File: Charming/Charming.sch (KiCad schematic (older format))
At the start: 9 parts, among them U1 proton_c

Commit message: sym4
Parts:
- removed U1: proton_c, symbol proton_c:proton_c
- added U1: ProMicro, Keebio-Parts:ArduinoProMicro, symbol keebio:ProMicro
- D1, D2, D3, D4: renamed from D?; footprint (none) -> Diode_SMD:D_SOD-123
- SW1, SW2, SW3, SW4: renamed from SW?; footprint (none) -> keyswitches:SW_PG1350
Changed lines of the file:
@@
 Comment4 ""
 $EndDescr
-$Comp
-L proton_c:proton_c U1
-U 1 1 5EE8D2D3
-P 2800 2100
-F 0 "U1" H 2775 577 50  0000 C CNN
-F 1 "proton_c" H 2775 486 50  0000 C CNN
-F 2 "" H 2650 2100 50  0001 C CNN
-F 3 "" H 2650 2100 50  0001 C CNN
-	1    2800 2100
-	1    0    0    -1
-$EndComp
 Wire Wire Line
 	4200 1400 3800 1400
@@
 L power:GND #PWR0102
 U 1 1 5EE91DD7
-P 1300 1600
-F 0 "#PWR0102" H 1300 1350 50  0001 C CNN
-F 1 "GND" H 1305 1427 50  0000 C CNN
-F 2 "" H 1300 1600 50  0001 C CNN
-F 3 "" H 1300 1600 50  0001 C CNN
-	1    1300 1600
-	1    0    0    -1
-$EndComp
-Wire Wire Line
-	1750 1300 1300 1300
-Wire Wire Line
-	1750 1400 1300 1400
-Wire Wire Line
-	1300 1300 1300 1400
+P 1950 1600
+F 0 "#PWR0102" H 1950 1350 50  0001 C CNN
+F 1 "GND" H 1955 1427 50  0000 C CNN
+F 2 "" H 1950 1600 50  0001 C CNN
+F 3 "" H 1950 1600 50  0001 C CNN
+	1    1950 1600
+	1    0    0    -1
+$EndComp
+Wire Wire Line
+	2400 1300 1950 1300
+Wire Wire Line
+	2400 1400 1950 1400
+Wire Wire Line
+	1950 1300 1950 1400
 $Comp
 L power:GND #PWR0103
@@
 L power:PWR_FLAG #FLG0102
 U 1 1 5EE952BC
-P 900 1650
-F 0 "#FLG0102" H 900 1725 50  0001 C CNN
-F 1 "PWR_FLAG" H 900 1823 50  0000 C CNN
-F 2 "" H 900 1650 50  0001 C CNN
-F 3 "~" H 900 1650 50  0001 C CNN
-	1    900  1650
+P 1550 1650
+F 0 "#FLG0102" H 1550 1725 50  0001 C CNN
+F 1 "PWR_FLAG" H 1550 1823 50  0000 C CNN
+F 2 "" H 1550 1650 50  0001 C CNN
+F 3 "~" H 1550 1650 50  0001 C CNN
+	1    1550 1650
 	1    0    0    -1
 $EndComp
@@
 	4200 1150 4200 1400
 Wire Wire Line
-	1300 1400 1300 1600
-Connection ~ 1300 1400
+	1950 1400 1950 1600
+Connection ~ 1950 1400
 $Comp
 L power:GND #PWR0104
 U 1 1 5EE95E75
-P 900 1750
-F 0 "#PWR0104" H 900 1500 50  0001 C CNN
-F 1 "GND" H 905 1577 50  0000 C CNN
-F 2 "" H 900 1750 50  0001 C CNN
-F 3 "" H 900 1750 50  0001 C CNN
-	1    900  1750
-	1    0    0    -1
-$EndComp
-Wire Wire Line
-	900  1650 900  1750
+P 1550 1750
+F 0 "#PWR0104" H 1550 1500 50  0001 C CNN
+F 1 "GND" H 1555 1577 50  0000 C CNN
+F 2 "" H 1550 1750 50  0001 C CNN
+F 3 "" H 1550 1750 50  0001 C CNN
+	1    1550 1750
+	1    0    0    -1
+$EndComp
+Wire Wire Line
+	1550 1650 1550 1750
 Wire Wire Line
 	4750 1250 4700 1250
@@
 	4750 900  4750 1250
 $Comp
-L Switch:SW_Push SW?
+L Switch:SW_Push SW1
 U 1 1 5EEA09FE
 P 4150 4900
-F 0 "SW?" H 4150 5185 50  0000 C CNN
+F 0 "SW1" H 4150 5185 50  0000 C CNN
 F 1 "SW_Push" H 4150 5094 50  0000 C CNN
-F 2 "" H 4150 5100 50  0001 C CNN
+F 2 "keyswitches:SW_PG1350" H 4150 5100 50  0001 C CNN
 F 3 "~" H 4150 5100 50  0001 C CNN
 	1    4150 4900
@@
 $EndComp
 $Comp
-L Switch:SW_Push SW?
+L Switch:SW_Push SW2
 U 1 1 5EEA0DB6
 P 4150 5600
-F 0 "SW?" H 4150 5885 50  0000 C CNN
+F 0 "SW2" H 4150 5885 50  0000 C CNN
 F 1 "SW_Push" H 4150 5794 50  0000 C CNN
-F 2 "" H 4150 5800 50  0001 C CNN
+F 2 "keyswitches:SW_PG1350" H 4150 5800 50  0001 C CNN
 F 3 "~" H 4150 5800 50  0001 C CNN
 	1    4150 5600
@@
 $EndComp
 $Comp
-L Switch:SW_Push SW?
+L Switch:SW_Push SW3
 U 1 1 5EEA10F4
 P 4900 4900
-F 0 "SW?" H 4900 5185 50  0000 C CNN
+F 0 "SW3" H 4900 5185 50  0000 C CNN
 F 1 "SW_Push" H 4900 5094 50  0000 C CNN
-F 2 "" H 4900 5100 50  0001 C CNN
+F 2 "keyswitches:SW_PG1350" H 4900 5100 50  0001 C CNN
 F 3 "~" H 4900 5100 50  0001 C CNN
 	1    4900 4900
@@
 $EndComp
 $Comp
-L Switch:SW_Push SW?
+L Switch:SW_Push SW4
 U 1 1 5EEA1601
 P 4900 5600
-F 0 "SW?" H 4900 5885 50  0000 C CNN
+F 0 "SW4" H 4900 5885 50  0000 C CNN
 F 1 "SW_Push" H 4900 5794 50  0000 C CNN
-F 2 "" H 4900 5800 50  0001 C CNN
+F 2 "keyswitches:SW_PG1350" H 4900 5800 50  0001 C CNN
 F 3 "~" H 4900 5800 50  0001 C CNN
 	1    4900 5600
@@
 	3950 4900 3950 5600
 $Comp
-L Device:D D?
+L Device:D D1
 U 1 1 5EEA2409
 P 4350 5050
-F 0 "D?" V 4396 4970 50  0000 R CNN
+F 0 "D1" V 4396 4970 50  0000 R CNN
 F 1 "D" V 4305 4970 50  0000 R CNN
-F 2 "" H 4350 5050 50  0001 C CNN
+F 2 "Diode_SMD:D_SOD-123" H 4350 5050 50  0001 C CNN
 F 3 "~" H 4350 5050 50  0001 C CNN
 	1    4350 5050
@@
 $EndComp
 $Comp
-L Device:D D?
+L Device:D D3
 U 1 1 5EEA2C67
 P 5100 5050
-F 0 "D?" V 5146 4970 50  0000 R CNN
+F 0 "D3" V 5146 4970 50  0000 R CNN
 F 1 "D" V 5055 4970 50  0000 R CNN
-F 2 "" H 5100 5050 50  0001 C CNN
+F 2 "Diode_SMD:D_SOD-123" H 5100 5050 50  0001 C CNN
 F 3 "~" H 5100 5050 50  0001 C CNN
 	1    5100 5050
@@
 $EndComp
 $Comp
-L Device:D D?
+L Device:D D2
 U 1 1 5EEA30D5
 P 4350 5750
-F 0 "D?" V 4396 5670 50  0000 R CNN
+F 0 "D2" V 4396 5670 50  0000 R CNN
 F 1 "D" V 4305 5670 50  0000 R CNN
-F 2 "" H 4350 5750 50  0001 C CNN
+F 2 "Diode_SMD:D_SOD-123" H 4350 5750 50  0001 C CNN
 F 3 "~" H 4350 5750 50  0001 C CNN
 	1    4350 5750
@@
 $EndComp
 $Comp
-L Device:D D?
+L Device:D D4
 U 1 1 5EEA33F4
 P 5100 5750
-F 0 "D?" V 5146 5670 50  0000 R CNN
+F 0 "D4" V 5146 5670 50  0000 R CNN
 F 1 "D" V 5055 5670 50  0000 R CNN
-F 2 "" H 5100 5750 50  0001 C CNN
+F 2 "Diode_SMD:D_SOD-123" H 5100 5750 50  0001 C CNN
 F 3 "~" H 5100 5750 50  0001 C CNN
 	1    5100 5750
@@
 Wire Wire Line
 	3800 1200 4350 1200
+Text GLabel 3800 1800 2    50   Input ~ 0
+col1
 Text GLabel 3800 1600 2    50   Input ~ 0
-col1
+row1
 Text GLabel 3800 1700 2    50   Input ~ 0
-row1
-Text GLabel 3800 1800 2    50   Input ~ 0
 col0
+$Comp
+L keebio:ProMicro U1
+U 1 1 5EEA488D
+P 3100 1650
+F 0 "U1" H 3100 2487 60  0000 C CNN
+F 1 "ProMicro" H 3100 2381 60  0000 C CNN
+F 2 "Keebio-Parts:ArduinoProMicro" V 4150 -850 60  0001 C CNN
+F 3 "" V 4150 -850 60  0001 C CNN
+	1    3100 1650
+	1    0    0    -1
+$EndComp
 $EndSCHEMATC

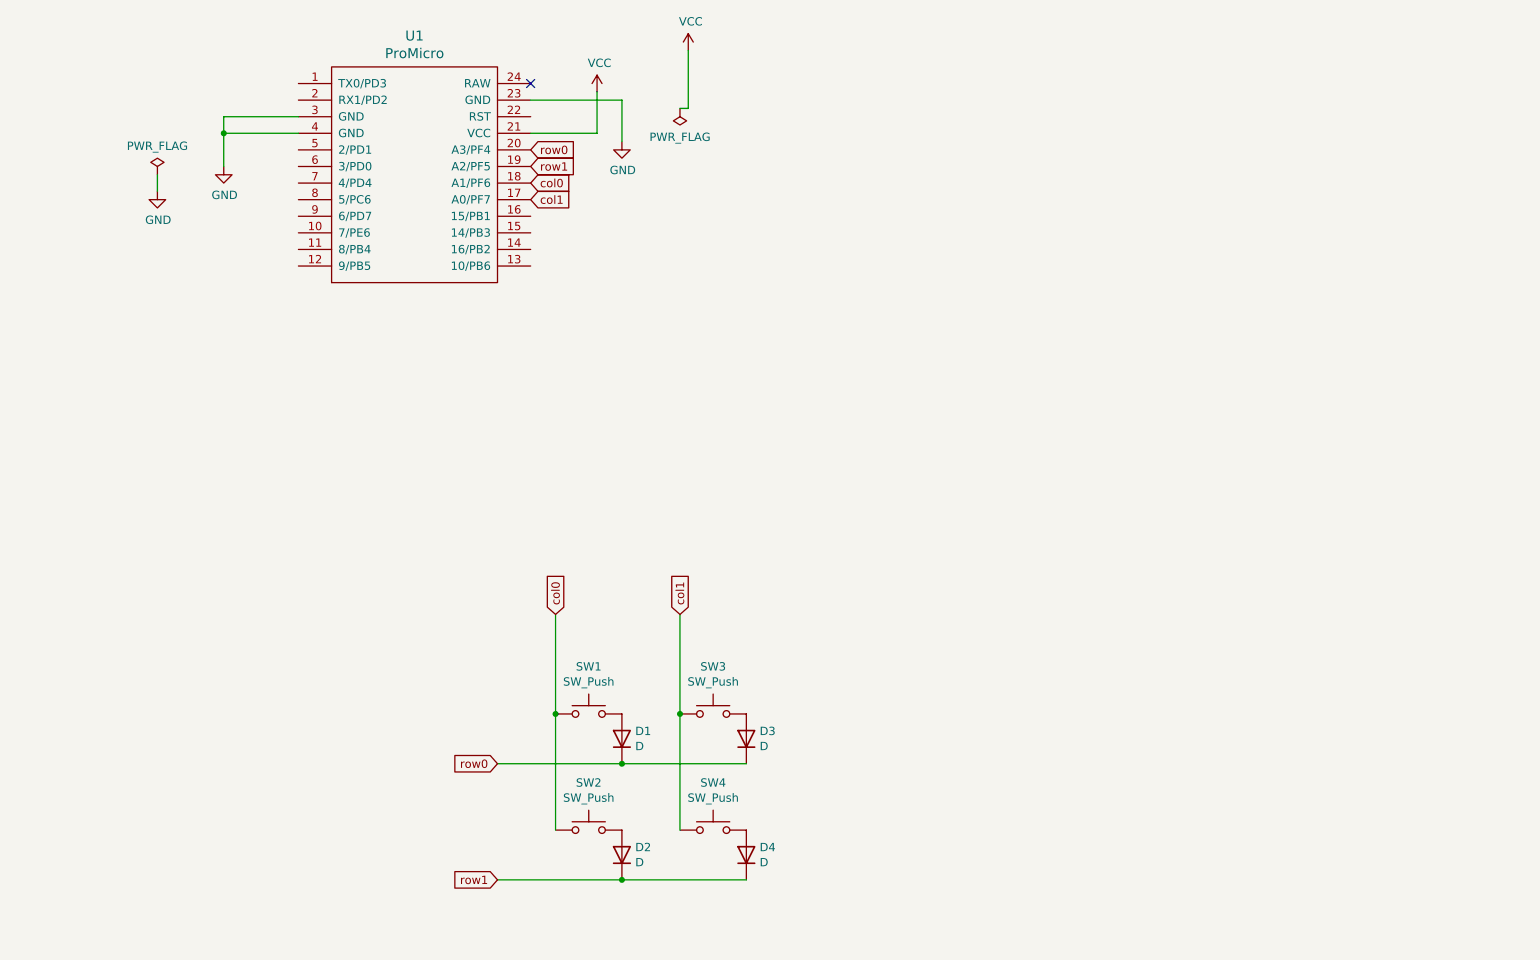
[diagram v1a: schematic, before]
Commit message: keyboard matrix ok
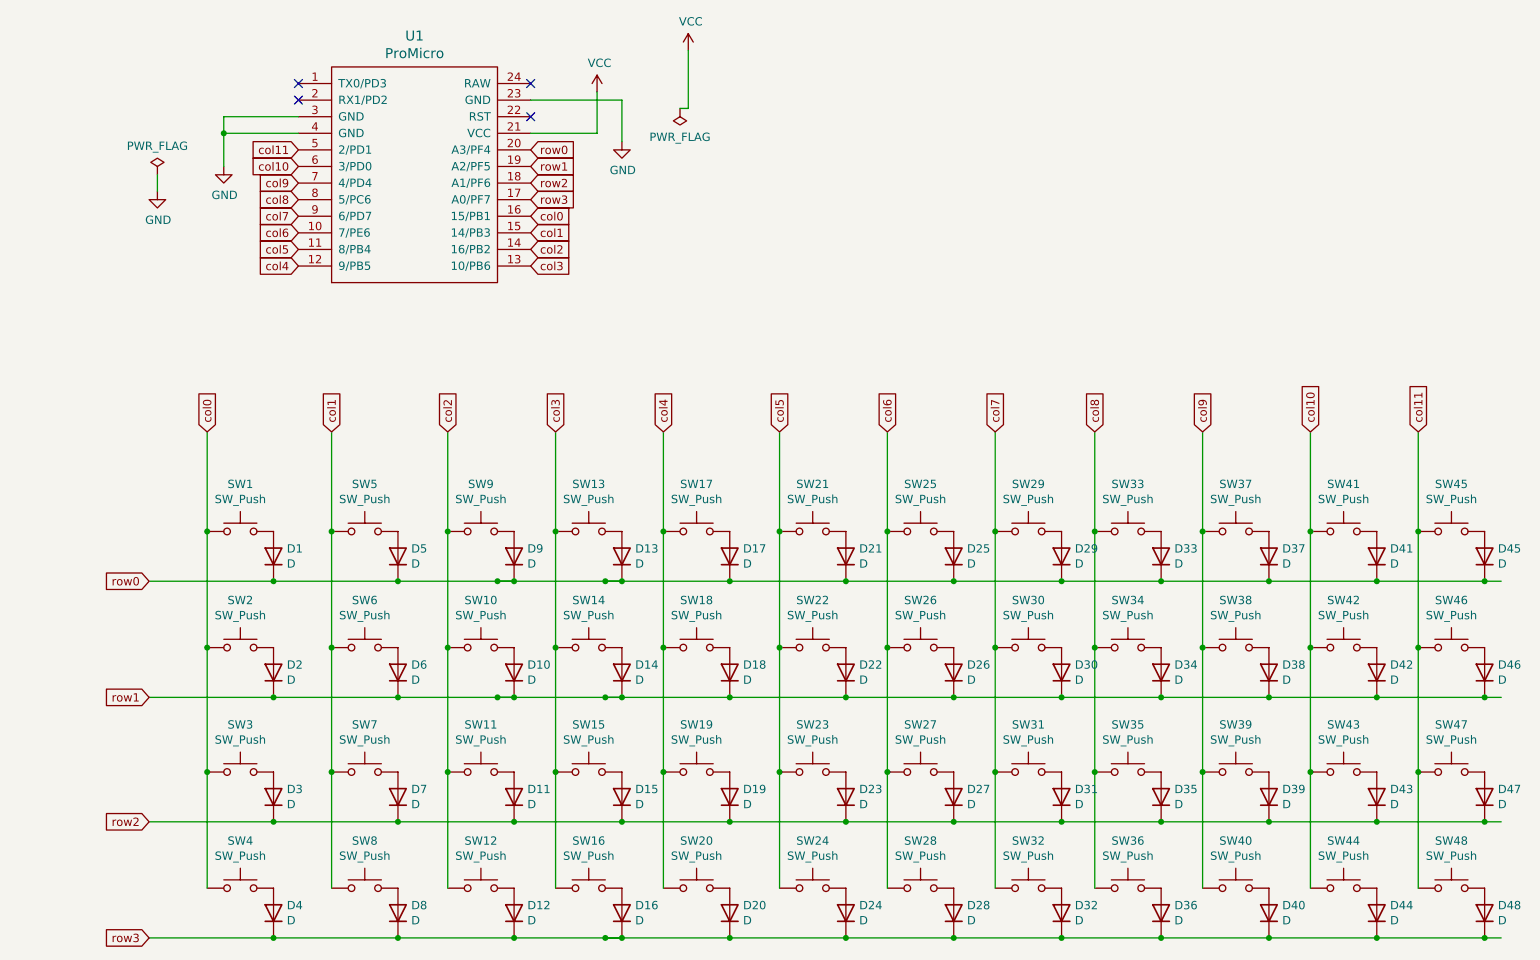
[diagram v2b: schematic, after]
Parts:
- added D10, D11, D12, D13, D14, D15, D16, D17, D18, D19, D20, D21, D22, D23, D24, D25, D26, D27, D28, D29, D3, D30, D31, D32, D33, D34, D35, D36, D37, D38, D39, D4, D40, D41, D42, D43, D44, D45, D46, D47, D48, D7, D8, D9: D, Diode_SMD:D_SOD-123, symbol Device:D
- added SW10, SW11, SW12, SW13, SW14, SW15, SW16, SW17, SW18, SW19, SW20, SW21, SW22, SW23, SW24, SW25, SW26, SW27, SW28, SW29, SW3, SW30, SW31, SW32, SW33, SW34, SW35, SW36, SW37, SW38, SW39, SW4, SW40, SW41, SW42, SW43, SW44, SW45, SW46, SW47, SW48, SW7, SW8, SW9: SW_Push, keyswitches:SW_PG1350, symbol Switch:SW_Push
- renumbered D3 to D5, D4 to D6, SW3 to SW5, SW4 to SW6
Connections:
- net labels added: col10, col11, col2, col3, col4, col5, col6, col7, col8, col9, row2, row3
- wire segments 19 -> 116
- no-connect marks 1 -> 4
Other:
- moved on the sheet: D1, D2, D5, D6, SW1, SW2, SW5, SW6

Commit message: update PG13500 footprint
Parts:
- SW1, SW10, SW11, SW12, SW13, SW14, SW15, SW16, SW17, SW18, SW19, SW2, SW20, SW21, SW22, SW23, SW24, SW25, SW26, SW27, SW28, SW29, SW3, SW30, SW31, SW32, SW33, SW34, SW35, SW36, SW37, SW38, SW39, SW4, SW40, SW41, SW42, SW43, SW44, SW45, SW46, SW47, SW48, SW5, SW6, SW7, SW8, SW9: footprint keyswitches:SW_PG1350 -> Charming:SW_PG1350

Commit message: before row col changle
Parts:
- renumbered D37 to D10, D41 to D11, D45 to D12, D2 to D13, D6 to D14, D10 to D15, D14 to D16, D18 to D17, D22 to D18, D26 to D19, D5 to D2, D30 to D20, D34 to D21, D38 to D22, D42 to D23, D46 to D24, D3 to D25, D7 to D26, D11 to D27, D15 to D28, D19 to D29, D9 to D3, D23 to D30, D27 to D31, D31 to D32, D35 to D33, D39 to D34, D43 to D35, D47 to D36, D4 to D37, D8 to D38, D12 to D39, D13 to D4, D16 to D40, D20 to D41, D24 to D42, D28 to D43, D32 to D44, D36 to D45, D40 to D46, D44 to D47, D17 to D5, D21 to D6, D25 to D7, D29 to D8, D33 to D9, SW37 to SW10, SW41 to SW11, SW45 to SW12, SW2 to SW13, SW6 to SW14, SW10 to SW15, SW14 to SW16, SW18 to SW17, SW22 to SW18, SW26 to SW19, SW5 to SW2, SW30 to SW20, SW34 to SW21, SW38 to SW22, SW42 to SW23, SW46 to SW24, SW3 to SW25, SW7 to SW26, SW11 to SW27, SW15 to SW28, SW19 to SW29, SW9 to SW3, SW23 to SW30, SW27 to SW31, SW31 to SW32, SW35 to SW33, SW39 to SW34, SW43 to SW35, SW47 to SW36, SW4 to SW37, SW8 to SW38, SW12 to SW39, SW13 to SW4, SW16 to SW40, SW20 to SW41, SW24 to SW42, SW28 to SW43, SW32 to SW44, SW36 to SW45, SW40 to SW46, SW44 to SW47, SW17 to SW5, SW21 to SW6, SW25 to SW7, SW29 to SW8, SW33 to SW9

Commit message: v1
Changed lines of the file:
@@
 Wire Wire Line
 	3800 1200 4350 1200
+Text GLabel 3800 1800 2    50   Input ~ 0
+col1
+Text GLabel 3800 1600 2    50   Input ~ 0
+row1
 Text GLabel 3800 1700 2    50   Input ~ 0
-col1
+col0
+Text GLabel 2400 2200 0    50   Input ~ 0
+row3
+Text GLabel 3800 1900 2    50   Input ~ 0
+col2
 Text GLabel 3800 2000 2    50   Input ~ 0
-row1
-Text GLabel 3800 1600 2    50   Input ~ 0
-col0
-Text GLabel 2400 1500 0    50   Input ~ 0
-row3
-Text GLabel 3800 1800 2    50   Input ~ 0
-col2
-Text GLabel 3800 1900 2    50   Input ~ 0
 col3
 Text GLabel 3800 2100 2    50   Input ~ 0
@@
 Text GLabel 3800 2200 2    50   Input ~ 0
 col5
-Text GLabel 2400 2200 0    50   Input ~ 0
+Text GLabel 2400 2000 0    50   Input ~ 0
 col6
-Text GLabel 2400 2100 0    50   Input ~ 0
+Text GLabel 2400 1900 0    50   Input ~ 0
 col7
-Text GLabel 2400 1900 0    50   Input ~ 0
+Text GLabel 2400 1800 0    50   Input ~ 0
 col8
-Text GLabel 2400 1800 0    50   Input ~ 0
+Text GLabel 2400 1700 0    50   Input ~ 0
 col9
-Text GLabel 2400 1700 0    50   Input ~ 0
+Text GLabel 2400 1600 0    50   Input ~ 0
 col10
-Text GLabel 2400 1600 0    50   Input ~ 0
+Text GLabel 2400 1500 0    50   Input ~ 0
 col11
 NoConn ~ 3800 1300
@@
 	1    0    0    -1
 $EndComp
-Text GLabel 2400 2000 0    50   Input ~ 0
+Text GLabel 2400 2100 0    50   Input ~ 0
 row2
 $Comp

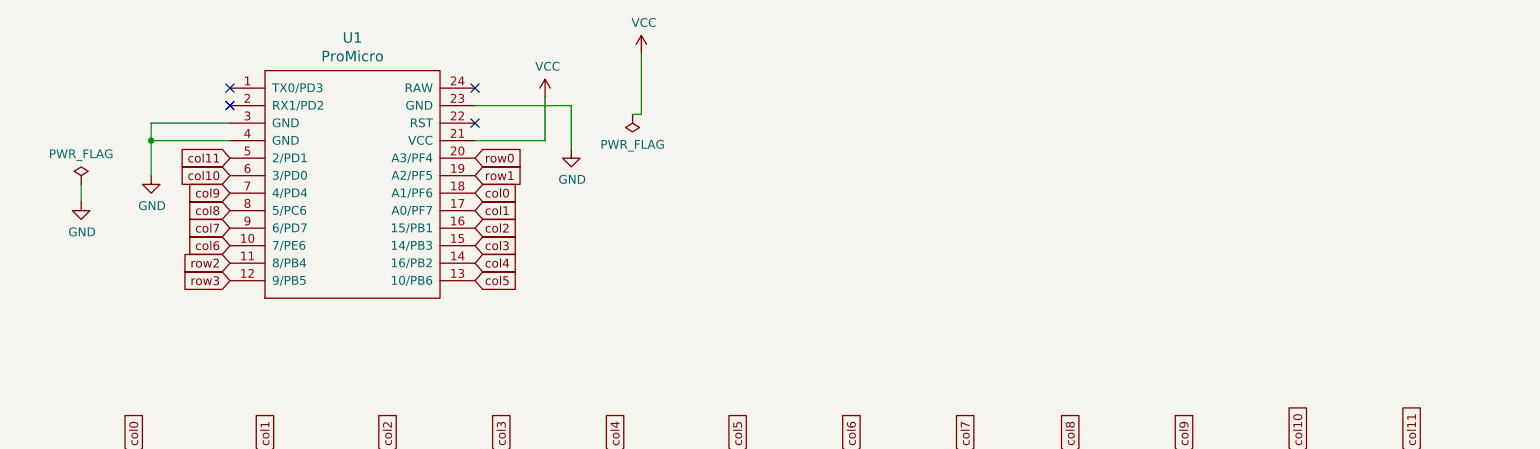
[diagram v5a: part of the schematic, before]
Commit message: change diode connector position
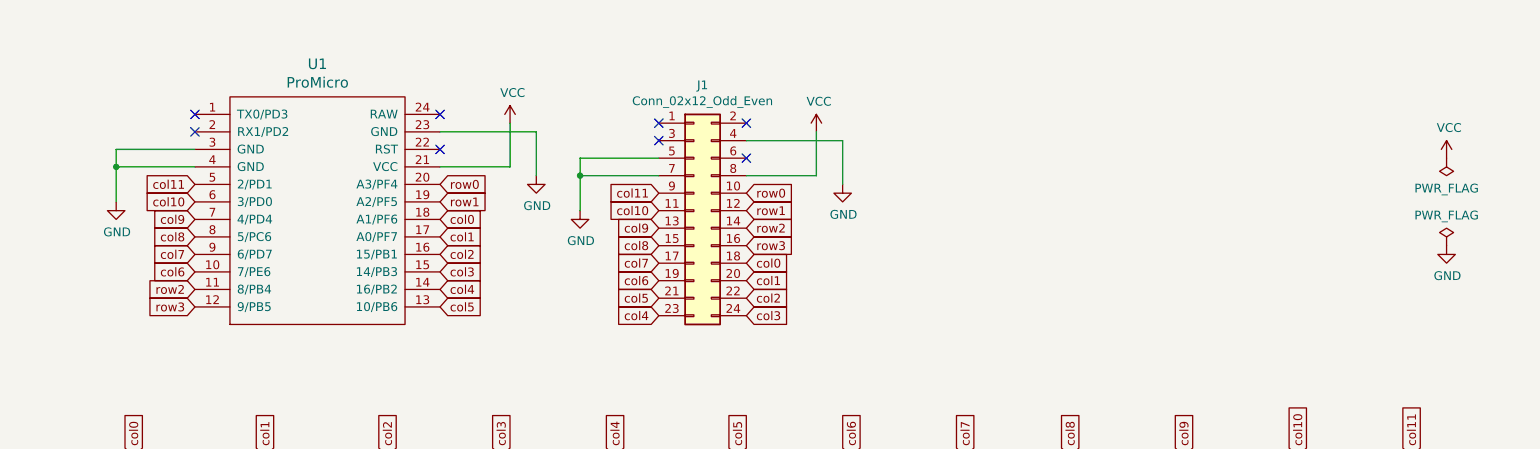
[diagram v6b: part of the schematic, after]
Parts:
- added J1: Conn_02x12_Odd_Even, Connector_PinSocket_2.54mm:PinSocket_2x12_P2.54mm_Vertical, symbol Connector_Generic:Conn_02x12_Odd_Even
- U1: footprint Keebio-Parts:ArduinoProMicro -> Connector_PinSocket_2.54mm:PinSocket_2x12_P2.54mm_Vertical
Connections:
- wire segments 116 -> 121
- no-connect marks 4 -> 8
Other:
- moved on the sheet: U1

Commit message: nice and clean signal lines
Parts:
- removed J1: Conn_02x12_Odd_Even, Connector_PinSocket_2.54mm:PinSocket_2x12_P2.54mm_Vertical, symbol Connector_Generic:Conn_02x12_Odd_Even
- D1: symbol Device:D -> Diode:1N4148W
- U1: footprint Connector_PinSocket_2.54mm:PinSocket_2x12_P2.54mm_Vertical -> Keebio:ArduinoProMicro
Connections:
- wire segments 121 -> 113
- no-connect marks 8 -> 4
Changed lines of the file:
@@
 Text GLabel 2200 2350 0    50   Input ~ 0
 row3
-Text GLabel 2200 2150 0    50   Input ~ 0
+Text GLabel 3600 2350 2    50   Input ~ 0
 col6
-Text GLabel 2200 2050 0    50   Input ~ 0
+Text GLabel 3600 2250 2    50   Input ~ 0
 col7
-Text GLabel 2200 1950 0    50   Input ~ 0
+Text GLabel 3600 2050 2    50   Input ~ 0
 col8
-Text GLabel 2200 1850 0    50   Input ~ 0
+Text GLabel 3600 1950 2    50   Input ~ 0
 col9
-Text GLabel 2200 1750 0    50   Input ~ 0
+Text GLabel 3600 1850 2    50   Input ~ 0
 col10
-Text GLabel 2200 1650 0    50   Input ~ 0
+Text GLabel 3600 1750 2    50   Input ~ 0
 col11
 NoConn ~ 3600 1450
@@
 	1850 3800 1850 4500
 $Comp
-L Device:D D1
+L Diode:1N4148W D1
 U 1 1 5EEA2409
 P 2250 3950
 F 0 "D1" V 2296 3870 50  0000 R CNN
-F 1 "D" V 2205 3870 50  0000 R CNN
+F 1 "D" V 2205 3870 50  0001 R CNN
 F 2 "Diode_SMD:D_SOD-123" H 2250 3950 50  0001 C CNN
 F 3 "~" H 2250 3950 50  0001 C CNN
@@
 	1    0    0    -1
 $EndComp
-Text GLabel 2200 2250 0    50   Input ~ 0
-row2
 $Comp
 L keebio:ProMicro U1
@@
 F 0 "U1" H 2900 2637 60  0000 C CNN
 F 1 "ProMicro" H 2900 2531 60  0000 C CNN
-F 2 "Connector_PinSocket_2.54mm:PinSocket_2x12_P2.54mm_Vertical" H 3950 -700 60  0001 C CNN
+F 2 "Keebio:ArduinoProMicro" H 3950 -700 60  0001 C CNN
 F 3 "" V 3950 -700 60  0001 C CNN
 	1    2900 1800
 	1    0    0    -1
 $EndComp
-Wire Wire Line
-	5750 1600 5350 1600
-$Comp
-L power:GND #PWR0101
-U 1 1 5EF07202
-P 5900 1650
-F 0 "#PWR0101" H 5900 1400 50  0001 C CNN
-F 1 "GND" H 5905 1477 50  0000 C CNN
-F 2 "" H 5900 1650 50  0001 C CNN
-F 3 "" H 5900 1650 50  0001 C CNN
-	1    5900 1650
-	1    0    0    -1
-$EndComp
-Wire Wire Line
-	5900 1400 5900 1650
-Wire Wire Line
-	5750 1350 5750 1600
-$Comp
-L power:VCC #PWR0102
-U 1 1 5EF0720A
-P 5750 1350
-F 0 "#PWR0102" H 5750 1200 50  0001 C CNN
-F 1 "VCC" H 5765 1523 50  0000 C CNN
-F 2 "" H 5750 1350 50  0001 C CNN
-F 3 "" H 5750 1350 50  0001 C CNN
-	1    5750 1350
-	1    0    0    -1
-$EndComp
-Wire Wire Line
-	5350 1400 5900 1400
-$Comp
-L power:GND #PWR0103
-U 1 1 5EF0E795
-P 4400 1800
-F 0 "#PWR0103" H 4400 1550 50  0001 C CNN
-F 1 "GND" H 4405 1627 50  0000 C CNN
-F 2 "" H 4400 1800 50  0001 C CNN
-F 3 "" H 4400 1800 50  0001 C CNN
-	1    4400 1800
-	1    0    0    -1
-$EndComp
-Wire Wire Line
-	4850 1500 4400 1500
-Wire Wire Line
-	4850 1600 4400 1600
-Wire Wire Line
-	4400 1500 4400 1600
-Wire Wire Line
-	4400 1600 4400 1800
-Connection ~ 4400 1600
-NoConn ~ 5350 1300
-NoConn ~ 5350 1500
-NoConn ~ 4850 1400
-NoConn ~ 4850 1300
-$Comp
-L Connector_Generic:Conn_02x12_Odd_Even J1
-U 1 1 5EF52355
-P 5050 1800
-F 0 "J1" H 5100 2517 50  0000 C CNN
-F 1 "Conn_02x12_Odd_Even" H 5100 2426 50  0000 C CNN
-F 2 "Connector_PinSocket_2.54mm:PinSocket_2x12_P2.54mm_Vertical" H 5050 1800 50  0001 C CNN
-F 3 "~" H 5050 1800 50  0001 C CNN
-	1    5050 1800
-	1    0    0    -1
-$EndComp
-Text GLabel 3600 2350 2    50   Input ~ 0
+Text GLabel 2200 2150 0    50   Input ~ 0
 col5
-Text GLabel 3600 2250 2    50   Input ~ 0
+Text GLabel 2200 2050 0    50   Input ~ 0
 col4
+Text GLabel 2200 1950 0    50   Input ~ 0
+col3
+Text GLabel 2200 1850 0    50   Input ~ 0
+col2
+Text GLabel 2200 1650 0    50   Input ~ 0
+col0
 Text GLabel 3600 2150 2    50   Input ~ 0
-col3
-Text GLabel 3600 2050 2    50   Input ~ 0
-col2
-Text GLabel 3600 1850 2    50   Input ~ 0
-col0
-Text GLabel 3600 1750 2    50   Input ~ 0
 row1
-Text GLabel 3600 1950 2    50   Input ~ 0
+Text GLabel 2200 1750 0    50   Input ~ 0
 col1
 Wire Wire Line
@@
 Wire Wire Line
 	4000 1550 3600 1550
-Text GLabel 5350 2400 2    50   Input ~ 0
-col3
-Text GLabel 5350 2300 2    50   Input ~ 0
-col2
-Text GLabel 5350 2100 2    50   Input ~ 0
-col0
-Text GLabel 5350 2200 2    50   Input ~ 0
-col1
-Text GLabel 5350 1900 2    50   Input ~ 0
+Text GLabel 2200 2250 0    50   Input ~ 0
 row2
-Text GLabel 5350 2000 2    50   Input ~ 0
-row3
-Text GLabel 5350 1800 2    50   Input ~ 0
-row1
-Text GLabel 5350 1700 2    50   Input ~ 0
-row0
-Text GLabel 4850 2200 0    50   Input ~ 0
-col6
-Text GLabel 4850 2100 0    50   Input ~ 0
-col7
-Text GLabel 4850 2000 0    50   Input ~ 0
-col8
-Text GLabel 4850 1900 0    50   Input ~ 0
-col9
-Text GLabel 4850 1800 0    50   Input ~ 0
-col10
-Text GLabel 4850 1700 0    50   Input ~ 0
-col11
-Text GLabel 4850 2300 0    50   Input ~ 0
-col5
-Text GLabel 4850 2400 0    50   Input ~ 0
-col4
 $EndSCHEMATC
